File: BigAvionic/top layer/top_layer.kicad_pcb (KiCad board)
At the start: 4 copper layers, 68 x 68 mm, 23 parts, among them J1 Conn_01x08, J2 Conn_Coaxial, J3 Conn_01x04, U1 NEO-M9N-00B, U2 MMC5983MA

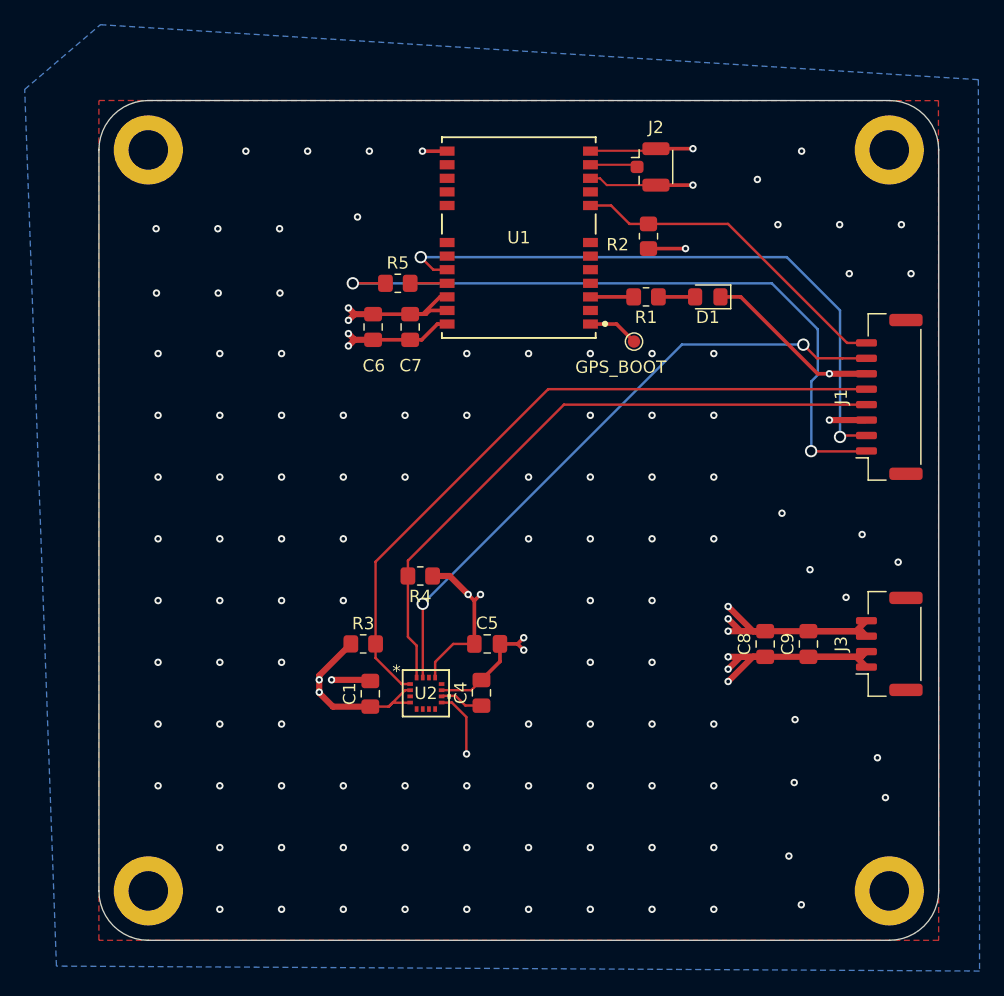
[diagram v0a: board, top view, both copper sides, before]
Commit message: add new power layer
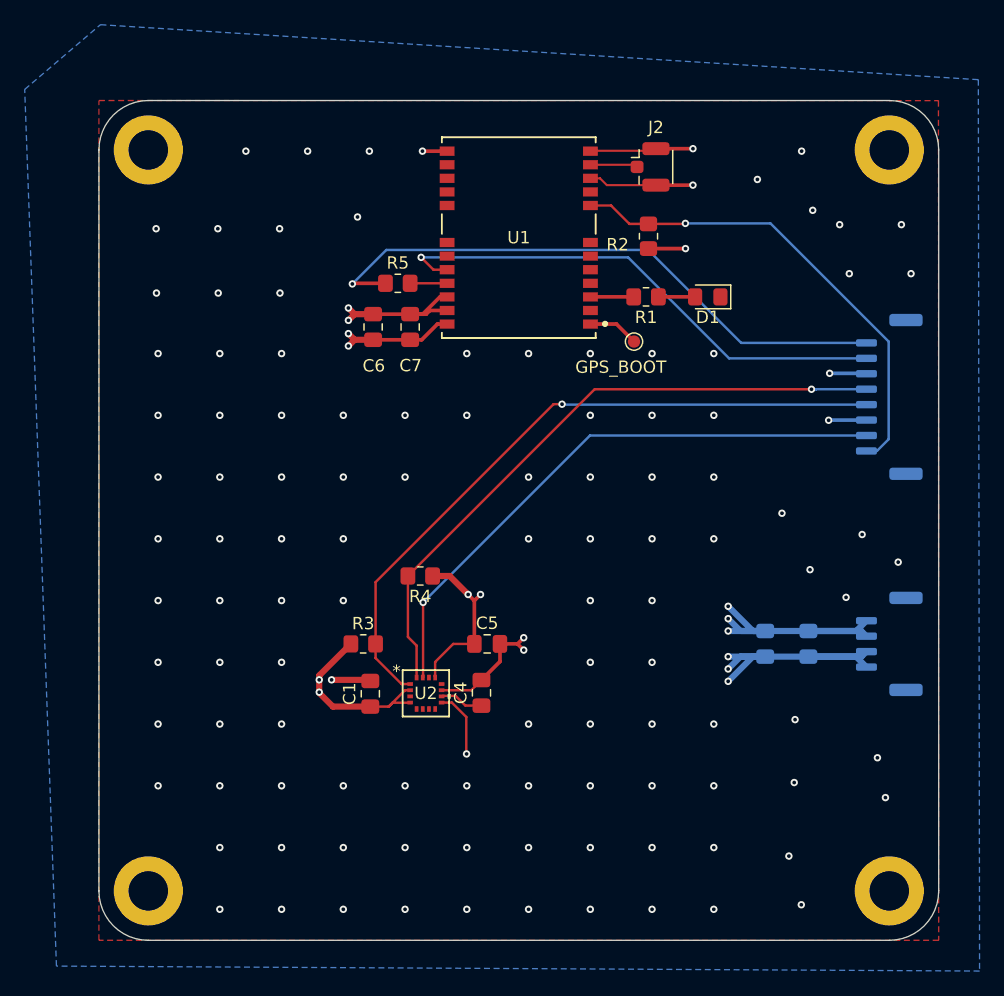
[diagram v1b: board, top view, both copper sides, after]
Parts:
- C8, C9, J1, J3: moved to B.Cu
- turned C8 to -90 degrees
- turned C9 to -90 degrees
- turned J3 to -90 degrees
- turned J1 to -90 degrees
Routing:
- net RST_GPS: track 27.0 -> 38.8 mm, vias 0 -> 1
- net GND: track 87.4 -> 76.1 mm
- net UART6_RX: track 50.7 -> 42.0 mm, vias 2 -> 1
- net UART6_TX: track 56.4 -> 48.6 mm, vias 2 -> 1
- net INT_Magn: track 51.1 -> 47.6 mm, vias 2 -> 1
- net I2C1_SCL: track 57.0 -> 55.5 mm, vias 0 -> 1
- net I2C1_SDA: track 52.1 -> 51.9 mm, vias 0 -> 1

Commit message: finish lora & top
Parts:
- added 3V3: TestPoint, TestPoint:TestPoint_Pad_D1.0mm, F.Cu at (140.8, 115.5)
- added D2: RED_LED, LED_SMD:LED_0805_2012Metric_Pad1.15x1.40mm_HandSolder, F.Cu at (145.9, 121.9)
- added GND1: TestPoint, TestPoint:TestPoint_Pad_D1.0mm, F.Cu at (140.8, 121.6)
- added R6: 1k, Resistor_SMD:R_0805_2012Metric_Pad1.20x1.40mm_HandSolder, F.Cu at (145.9, 117.5)
- moved J2 0.39 mm to (143.0, 78.5)
- renumbered GPS_BOOT to TP1
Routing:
- net +3.3V: track 68.0 -> 53.1 mm, vias 10 -> 7
- net GND: track 76.1 -> 62.1 mm, vias 122 -> 146
- net Net-(D2-A): track 0.00 -> 2.34 mm
- added copper zone on B.Cu, net +3.3V

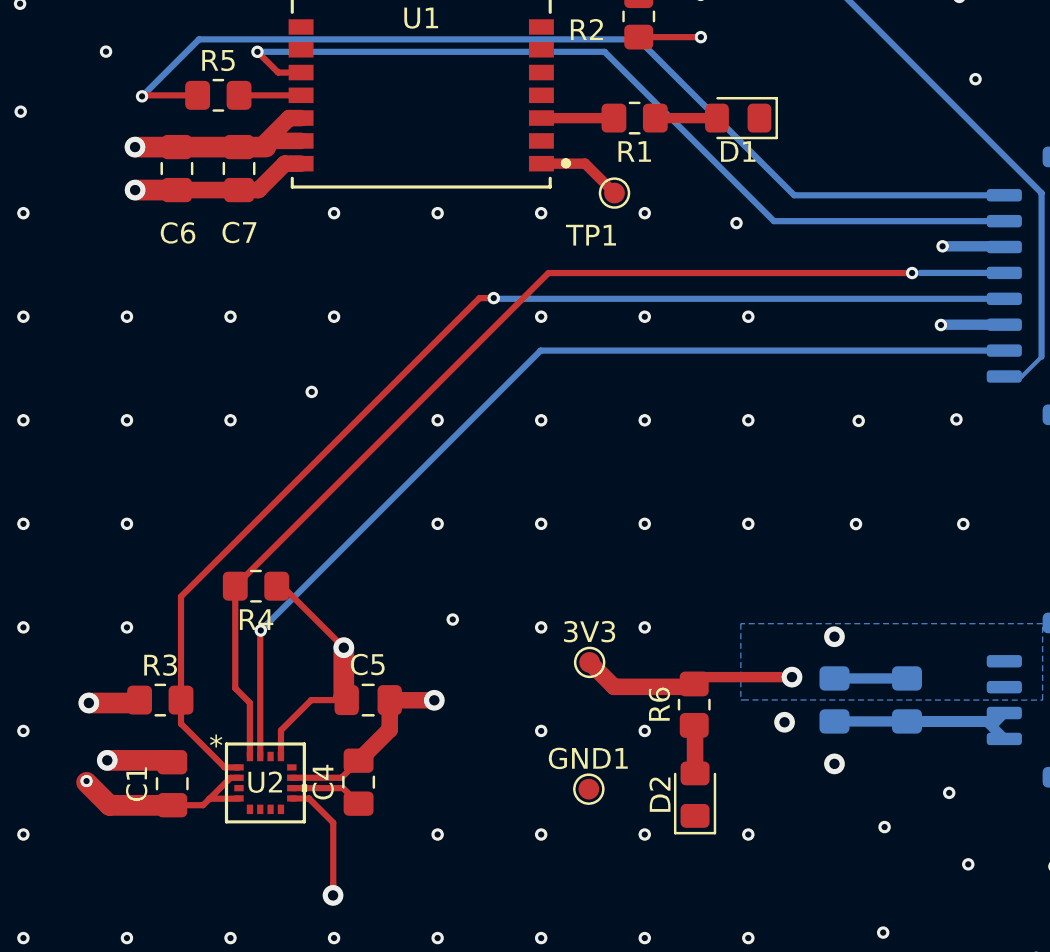
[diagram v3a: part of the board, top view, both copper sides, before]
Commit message: check lora top power generate garber
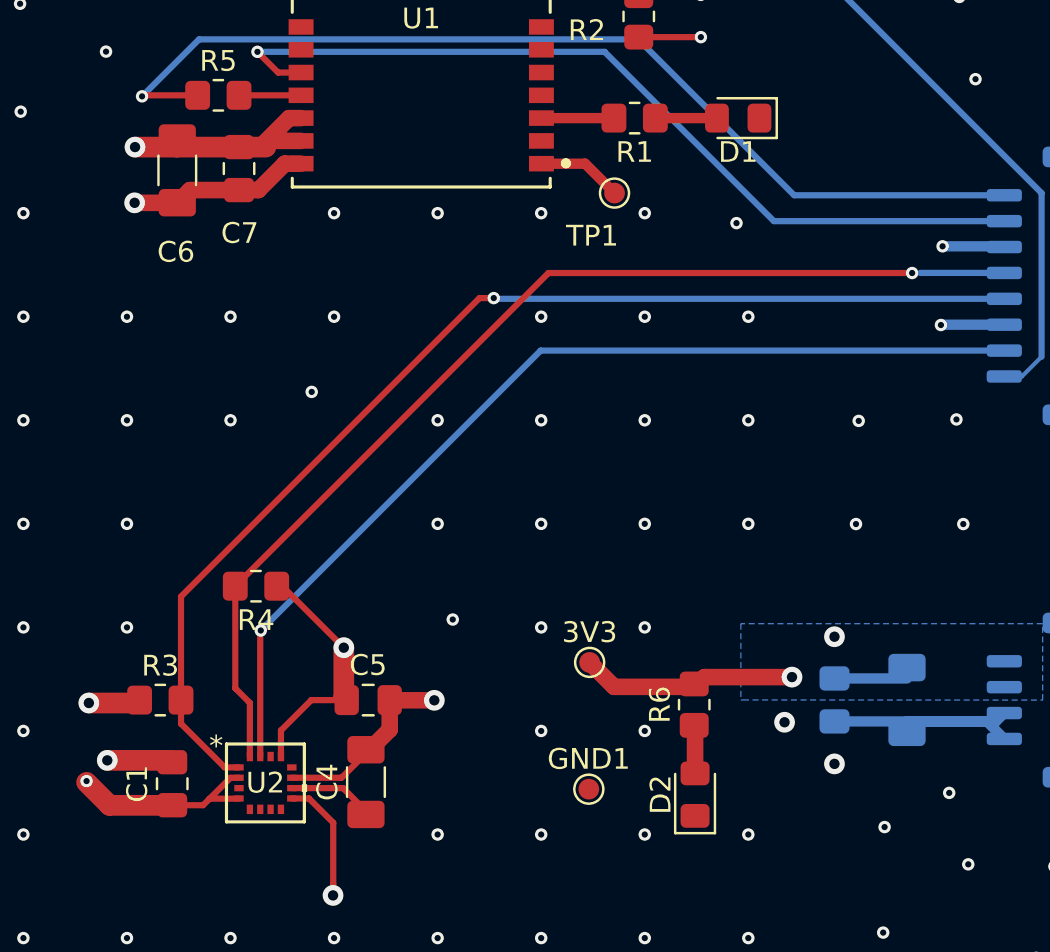
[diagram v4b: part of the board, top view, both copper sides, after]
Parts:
- C4, C6, C9: footprint Capacitor_SMD:C_0805_2012Metric_Pad1.18x1.45mm_HandSolder -> Capacitor_SMD:C_1206_3216Metric_Pad1.33x1.80mm_HandSolder
- moved C4 0.36 mm to (130.0, 121.3)
- moved C6 0.09 mm to (120.9, 91.7)
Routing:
- net Net-(U2-CAP): track 3.54 -> 4.21 mm

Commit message: MCU process
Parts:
- turned C8 to 90 degrees
- turned C9 to 90 degrees
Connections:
- J3 pad 1: +3.3V -> GND
- J3 pad 2: +3.3V -> GND
- J3 pad 3: GND -> +3.3V
- J3 pad 4: GND -> +3.3V
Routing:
- net +3.3V: track 53.1 -> 63.3 mm
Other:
- board text added: "P_TOP"
- board text added: "S_TOP"

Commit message: MCU layer progress 1
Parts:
- added D3: TVS, Diode_SMD:D_SMA, B.Cu at (157.8, 125.1)
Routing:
- net +3.3V: track 63.3 -> 69.1 mm
